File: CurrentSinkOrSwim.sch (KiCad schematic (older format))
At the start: 16 parts

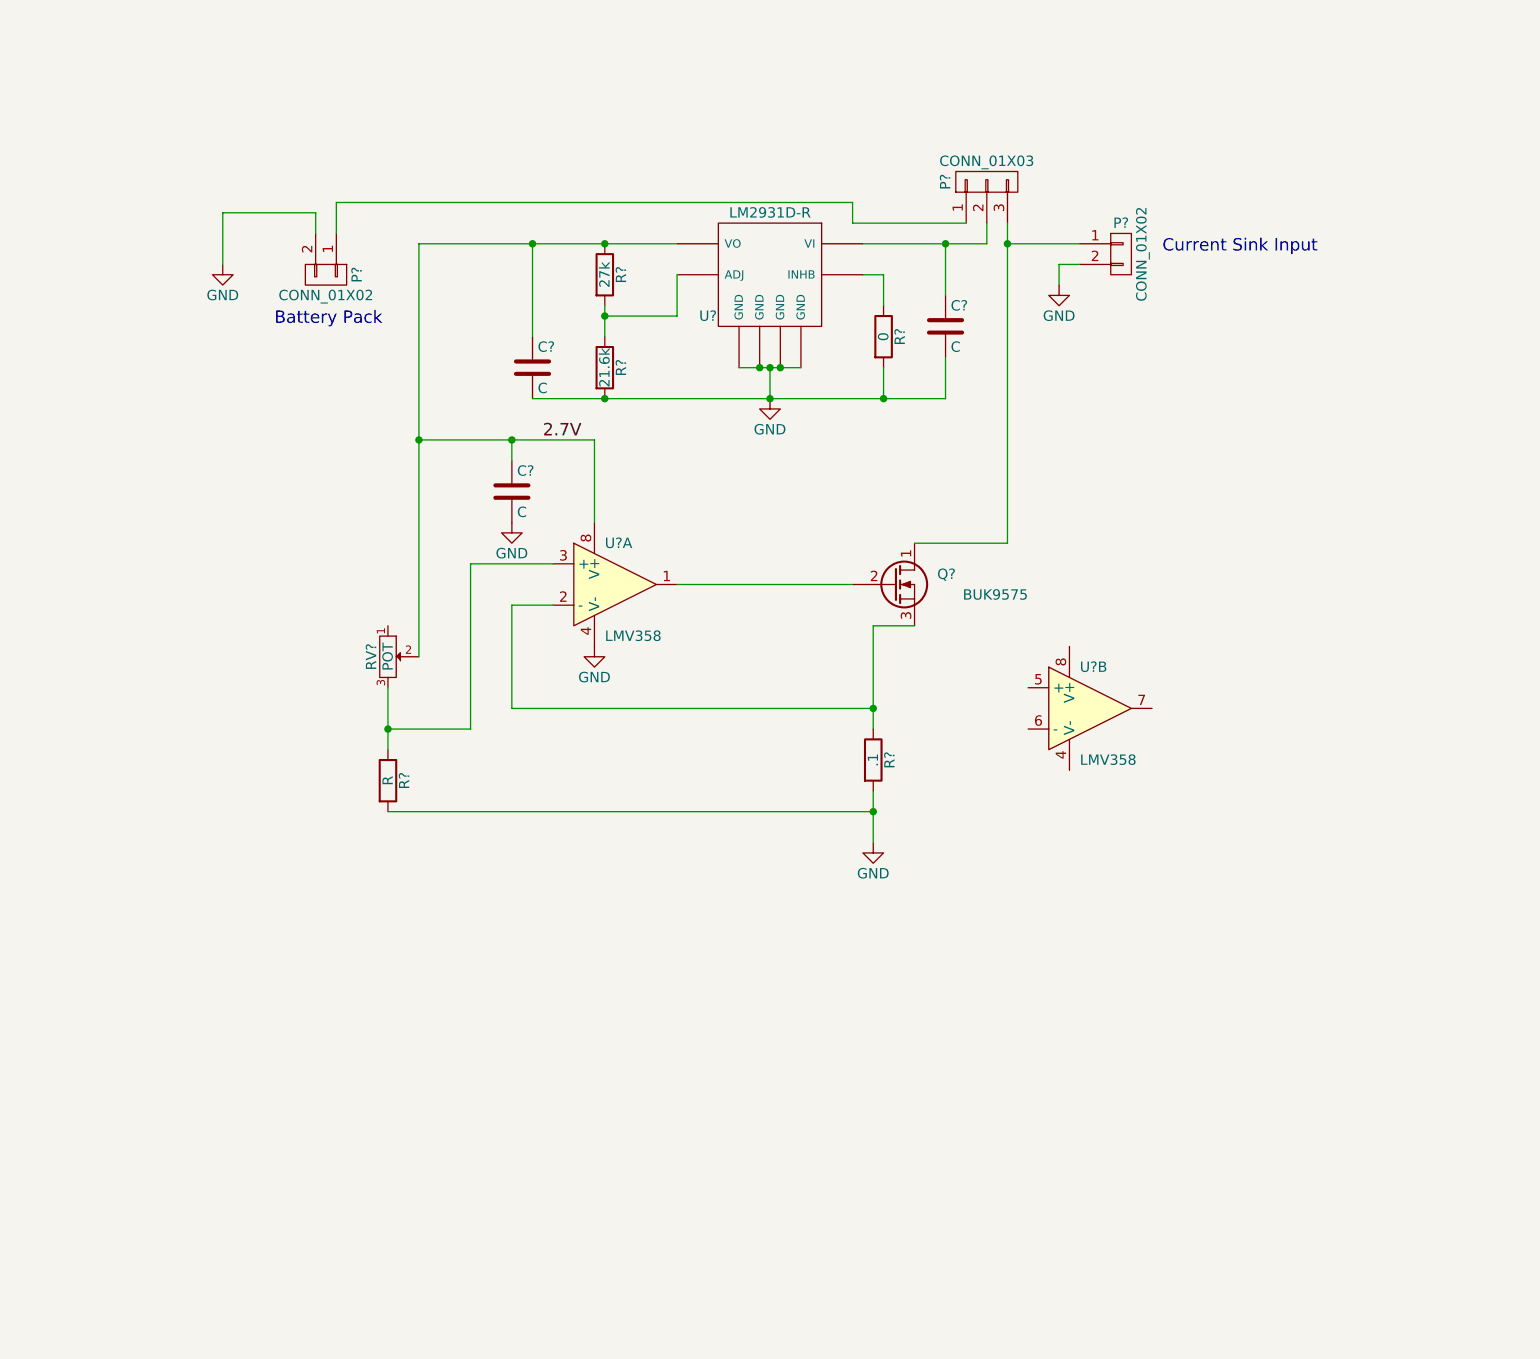
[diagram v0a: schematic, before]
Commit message: Create hierarchical sheets
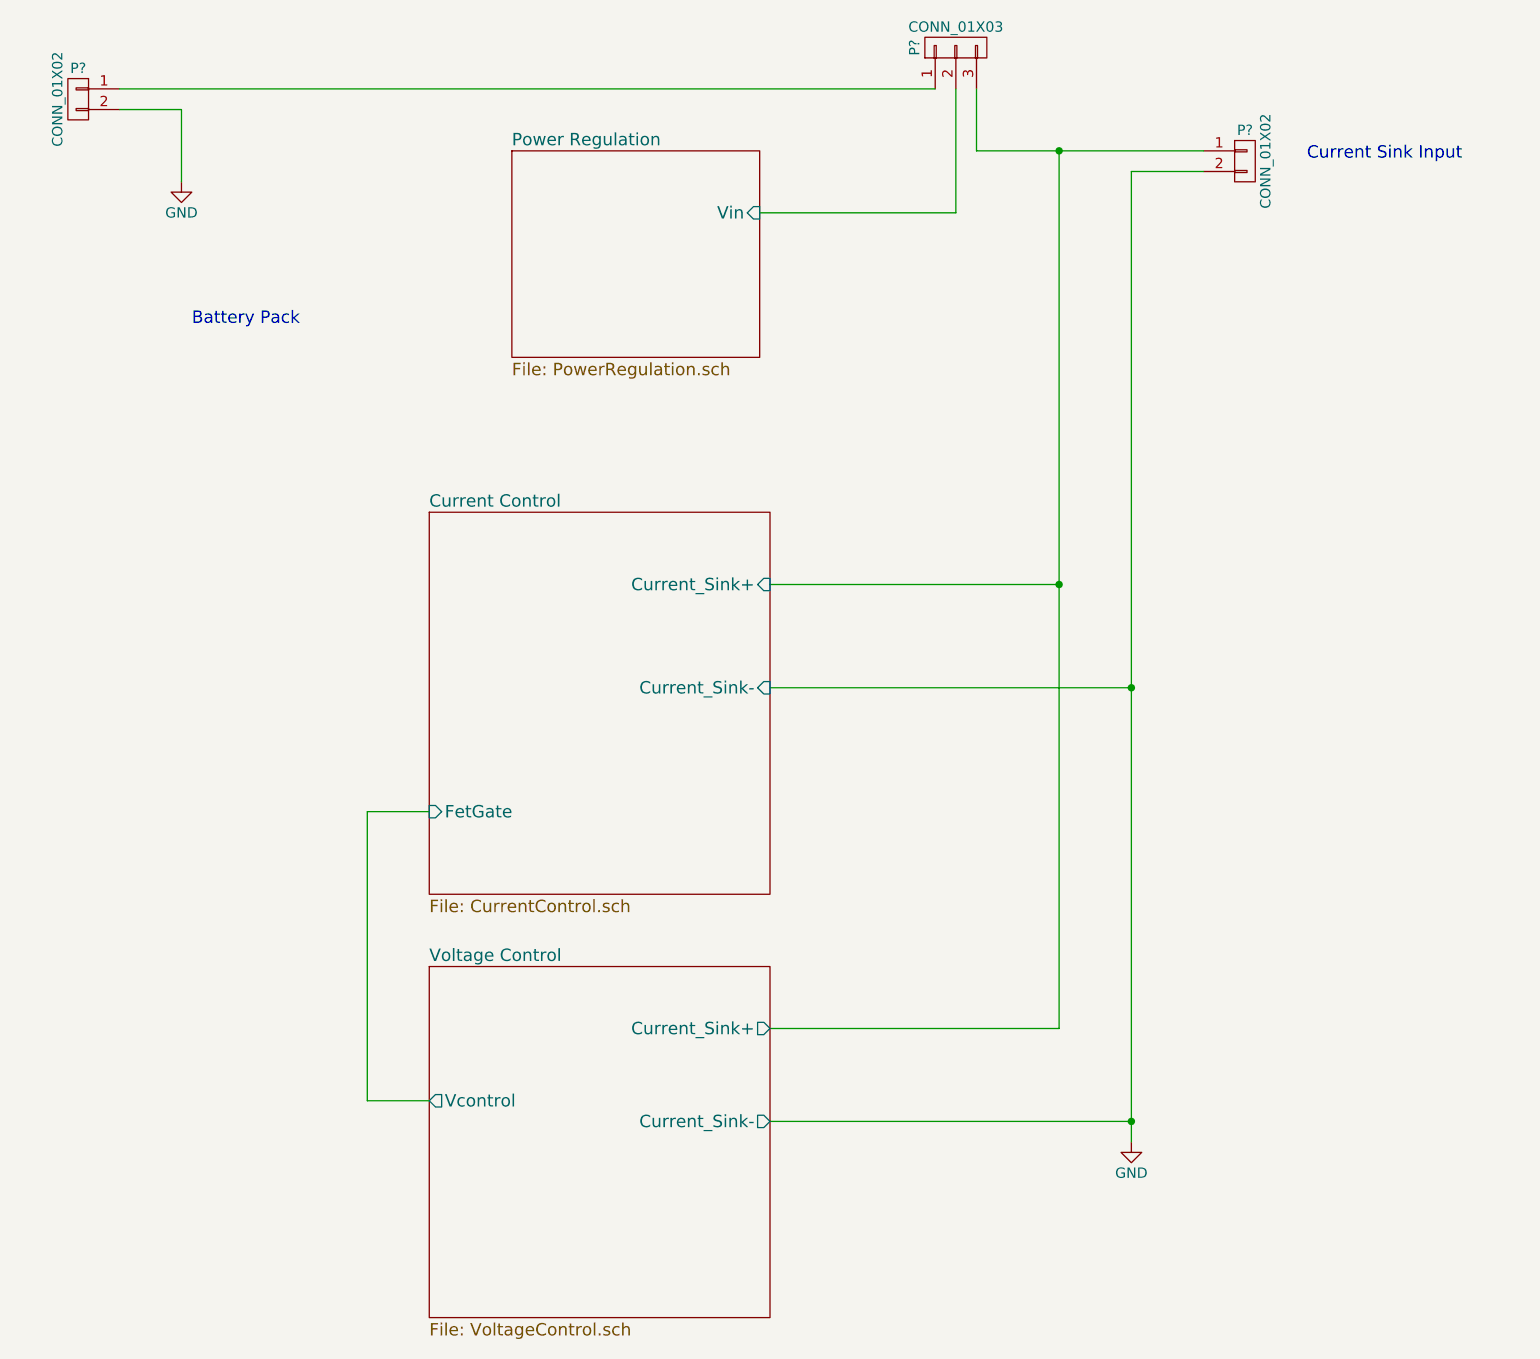
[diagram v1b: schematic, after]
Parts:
- removed C? (x3): C, symbol C
- removed Q?: BUK9575, symbol Q_NMOS_DGS
- removed R?: R, symbol R
- removed R?: .1, symbol R
- removed R?: 0, symbol R
- removed R?: 27k, symbol R
- removed R?: 21.6k, symbol R
- removed RV?: POT, symbol POT
- removed U? (x2): LMV358, symbol LMV358
- removed U?: LM2931D-R, symbol LM2931D-R
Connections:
- net Current Control/Current_Sink+: now reaches P?.1 (P1), P?.3 (P3)
- net Power Regulation/Vin: now reaches P?.2 (P2)
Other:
- moved on the sheet: P?

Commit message: Annotation completed
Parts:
- gave numbers to parts that had none: 3
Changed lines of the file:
@@
 $EndDescr
 $Comp
-L CONN_01X02 P?
+L CONN_01X02 P103
 U 1 1 57C1F29D
 P 8350 1550
-F 0 "P?" H 8350 1700 50  0000 C CNN
+F 0 "P103" H 8350 1700 50  0000 C CNN
 F 1 "CONN_01X02" V 8450 1550 50  0000 C CNN
 F 2 "" H 8350 1550 50  0000 C CNN
@@
 $EndComp
 $Comp
-L CONN_01X03 P?
+L CONN_01X03 P102
 U 1 1 57D502F2
 P 6950 1000
-F 0 "P?" H 6950 1200 50  0000 C CNN
+F 0 "P102" H 6950 1200 50  0000 C CNN
 F 1 "CONN_01X03" V 7050 1000 50  0000 C CNN
 F 2 "" H 6950 1000 50  0000 C CNN
@@
 $EndComp
 $Comp
-L CONN_01X02 P?
+L CONN_01X02 P101
 U 1 1 57D5050E
 P 2700 1250
-F 0 "P?" H 2700 1400 50  0000 C CNN
+F 0 "P101" H 2700 1400 50  0000 C CNN
 F 1 "CONN_01X02" V 2800 1250 50  0000 C CNN
 F 2 "" H 2700 1250 50  0000 C CNN
@@
 $EndComp
 $Comp
-L GND #PWR?
+L GND #PWR101
 U 1 1 57D507BE
 P 3200 1650
-F 0 "#PWR?" H 3200 1400 50  0001 C CNN
+F 0 "#PWR101" H 3200 1400 50  0001 C CNN
 F 1 "GND" H 3200 1500 50  0000 C CNN
 F 2 "" H 3200 1650 50  0000 C CNN
@@
 	1    0    0    -1
 $EndComp
-Text Notes 3250 2350 0    60   ~ 0
+Text Notes 2400 1650 0    60   ~ 0
 Battery Pack
 Text Notes 8650 1550 0    60   ~ 0
 Current Sink Input
 $Sheet
-S 4400 3250 1650 1850
+S 4400 3250 1600 1550
 U 57DA07A1
 F0 "Current Control" 60
 F1 "CurrentControl.sch" 60
-F2 "FetGate" I L 4400 4700 60
-F3 "Current_Sink+" I R 6050 3600 60
-F4 "Current_Sink-" I R 6050 4100 60
+F2 "FetGate" I L 4400 4400 60
+F3 "Current_Sink+" I R 6000 3600 60
+F4 "Current_Sink-" I R 6000 4100 60
 $EndSheet
 $Sheet
-S 4400 5450 1650 1700
+S 4400 5050 1600 1700
 U 57DA0A56
 F0 "Voltage Control" 60
 F1 "VoltageControl.sch" 60
-F2 "Vcontrol" O L 4400 6100 60
-F3 "Current_Sink+" O R 6050 5750 60
-F4 "Current_Sink-" O R 6050 6200 60
+F2 "Vcontrol" O L 4400 5700 60
+F3 "Current_Sink+" O R 6000 5350 60
+F4 "Current_Sink-" O R 6000 5800 60
 $EndSheet
 $Sheet
@@
 $EndSheet
 $Comp
-L GND #PWR?
+L GND #PWR102
 U 1 1 57DB9B88
-P 7800 6300
-F 0 "#PWR?" H 7800 6050 50  0001 C CNN
-F 1 "GND" H 7800 6150 50  0000 C CNN
-F 2 "" H 7800 6300 50  0000 C CNN
-F 3 "" H 7800 6300 50  0000 C CNN
-	1    7800 6300
+P 7800 6000
+F 0 "#PWR102" H 7800 5750 50  0001 C CNN
+F 1 "GND" H 7800 5850 50  0000 C CNN
+F 2 "" H 7800 6000 50  0000 C CNN
+F 3 "" H 7800 6000 50  0000 C CNN
+	1    7800 6000
 	1    0    0    -1
 $EndComp
 Wire Wire Line
-	7800 1600 7800 6300
+	7800 1600 7800 6000
 Wire Wire Line
 	7800 1600 8150 1600
@@
 	7050 1500 8150 1500
 Wire Wire Line
-	7450 1500 7450 5750
+	7450 1500 7450 5350
 Wire Wire Line
 	6050 3600 7450 3600
@@
 	6950 1800 6000 1800
 Wire Wire Line
-	7450 5750 6050 5750
+	7450 5350 5950 5350
 Connection ~ 7450 3600
-Wire Wire Line
-	7800 6200 6050 6200
 Connection ~ 7800 4100
 Wire Wire Line
-	4400 6100 4100 6100
+	4100 5700 4100 4400
 Wire Wire Line
-	4100 6100 4100 4700
-Wire Wire Line
-	4100 4700 4400 4700
-Connection ~ 7800 6200
+	4100 4400 4400 4400
 Wire Wire Line
 	2900 1300 3200 1300
@@
 	2900 1200 6850 1200
 Connection ~ 7450 1500
+Wire Wire Line
+	6000 5800 7800 5800
+Connection ~ 7800 5800
+Wire Wire Line
+	4400 5700 4100 5700
 $EndSCHEMATC

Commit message: Add initial layout
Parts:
- P101, P103: footprint (none) -> Pin_Headers:Pin_Header_Angled_1x02
- P102: footprint (none) -> Pin_Headers:Pin_Header_Angled_1x03
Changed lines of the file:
@@
 F 0 "P103" H 8350 1700 50  0000 C CNN
 F 1 "CONN_01X02" V 8450 1550 50  0000 C CNN
-F 2 "" H 8350 1550 50  0000 C CNN
+F 2 "Pin_Headers:Pin_Header_Angled_1x02" H 8350 1550 50  0001 C CNN
 F 3 "" H 8350 1550 50  0000 C CNN
 	1    8350 1550
@@
 F 0 "P102" H 6950 1200 50  0000 C CNN
 F 1 "CONN_01X03" V 7050 1000 50  0000 C CNN
-F 2 "" H 6950 1000 50  0000 C CNN
+F 2 "Pin_Headers:Pin_Header_Angled_1x03" H 6950 1000 50  0001 C CNN
 F 3 "" H 6950 1000 50  0000 C CNN
 	1    6950 1000
@@
 F 0 "P101" H 2700 1400 50  0000 C CNN
 F 1 "CONN_01X02" V 2800 1250 50  0000 C CNN
-F 2 "" H 2700 1250 50  0000 C CNN
+F 2 "Pin_Headers:Pin_Header_Angled_1x02" H 2700 1250 50  0001 C CNN
 F 3 "" H 2700 1250 50  0000 C CNN
 	1    2700 1250
@@
 $EndComp
 $Comp
-L GND #PWR101
+L GND #PWR01
 U 1 1 57D507BE
 P 3200 1650
-F 0 "#PWR101" H 3200 1400 50  0001 C CNN
+F 0 "#PWR01" H 3200 1400 50  0001 C CNN
 F 1 "GND" H 3200 1500 50  0000 C CNN
 F 2 "" H 3200 1650 50  0000 C CNN
@@
 $EndSheet
 $Comp
-L GND #PWR102
+L GND #PWR02
 U 1 1 57DB9B88
 P 7800 6000
-F 0 "#PWR102" H 7800 5750 50  0001 C CNN
+F 0 "#PWR02" H 7800 5750 50  0001 C CNN
 F 1 "GND" H 7800 5850 50  0000 C CNN
 F 2 "" H 7800 6000 50  0000 C CNN

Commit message: Add potentiometers
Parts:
- P101, P103: footprint Pin_Headers:Pin_Header_Angled_1x02 -> current:Terminal_Block_200_mil; MPN (none) -> OSTTC022162
- P102: footprint Pin_Headers:Pin_Header_Angled_1x03 -> Pin_Headers:Pin_Header_Straight_1x03
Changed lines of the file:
@@
 F 0 "P103" H 8350 1700 50  0000 C CNN
 F 1 "CONN_01X02" V 8450 1550 50  0000 C CNN
-F 2 "Pin_Headers:Pin_Header_Angled_1x02" H 8350 1550 50  0001 C CNN
-F 3 "" H 8350 1550 50  0000 C CNN
+F 2 "current:Terminal_Block_200_mil" H 8350 1550 50  0001 C CNN
+F 3 "http://www.on-shore.com/wp-content/uploads/2015/09/osttcxx2162.pdf" H 8350 1550 50  0001 C CNN
+F 4 "OSTTC022162" H 8350 1550 60  0001 C CNN "MPN"
 	1    8350 1550
 	1    0    0    -1
@@
 F 0 "P102" H 6950 1200 50  0000 C CNN
 F 1 "CONN_01X03" V 7050 1000 50  0000 C CNN
-F 2 "Pin_Headers:Pin_Header_Angled_1x03" H 6950 1000 50  0001 C CNN
+F 2 "Pin_Headers:Pin_Header_Straight_1x03" H 6950 1000 50  0001 C CNN
 F 3 "" H 6950 1000 50  0000 C CNN
 	1    6950 1000
@@
 F 0 "P101" H 2700 1400 50  0000 C CNN
 F 1 "CONN_01X02" V 2800 1250 50  0000 C CNN
-F 2 "Pin_Headers:Pin_Header_Angled_1x02" H 2700 1250 50  0001 C CNN
-F 3 "" H 2700 1250 50  0000 C CNN
+F 2 "current:Terminal_Block_200_mil" H 2700 1250 50  0001 C CNN
+F 3 "http://www.on-shore.com/wp-content/uploads/2015/09/osttcxx2162.pdf" H 2700 1250 50  0001 C CNN
+F 4 "OSTTC022162" H 2700 1250 60  0001 C CNN "MPN"
 	1    2700 1250
 	-1   0    0    -1

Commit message: Lets try layout one more time. Starting layout from scratch
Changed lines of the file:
@@
 	7450 1500 7450 5350
 Wire Wire Line
-	6050 3600 7450 3600
+	6000 3600 7450 3600
 Wire Wire Line
-	6050 4100 7800 4100
+	6000 4100 7800 4100
 Wire Wire Line
 	6950 1800 6000 1800
 Wire Wire Line
-	7450 5350 5950 5350
+	7450 5350 6000 5350
 Connection ~ 7450 3600
 Connection ~ 7800 4100

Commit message: Final schematic and BOM and layout
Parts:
- P102: MPN (none) -> 68000-103HLF
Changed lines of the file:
@@
 F 1 "CONN_01X03" V 7050 1000 50  0000 C CNN
 F 2 "Pin_Headers:Pin_Header_Straight_1x03" H 6950 1000 50  0001 C CNN
-F 3 "" H 6950 1000 50  0000 C CNN
+F 3 "http://portal.fciconnect.com/Comergent//fci/drawing/68000.pdf" H 6950 1000 50  0001 C CNN
+F 4 "68000-103HLF" H 6950 1000 60  0001 C CNN "MPN"
 	1    6950 1000
 	0    -1   -1   0
